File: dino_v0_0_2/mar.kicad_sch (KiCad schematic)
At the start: 5 parts, among them U54 74LS245, U55 74LS373

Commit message: feat(dino): complete v0.0.3 schematic — all 11 sheets netlist-clean
- wire MAR sheet: '373 LO/HI latches, 2x '245 M-bus drive, A15 decode
  (ROM_EN/~RAM_EN), LE stamps off /MAR_LO_LOAD//MAR_HI_LOAD
- fix PC_MAR_MUX polarity: PC '245s enabled on bit14=0, inverted vs
  bit-map convention (PC=1); add ~PC_MAR_MUX inverter, relabel U13/U14
- wire all 7 control-word bus taps [15:9] (SA0-2, END, PC_UP,
  PC_MAR_MUX, HALT) — label pairs had no wire between them
- untie NONE/NC '138 outputs: totem-pole bus fight on every microword;
  each unused output now individually no_connect
- build END (U61 NOR: ~MR = RESET|END, sync T-state clear) and HALT
  (T-state freeze via CET, clock keeps running)
- build COND/JNZ (U62: ~PC_LOAD = taken-JNZ | unconditional-JMP)
- claim src code 111 as /SW_OUT: IN port — DIP switches through 10k
  pull-ups onto W bus via '244; LED bank active-high off OB0-7
- add U66 missing power unit + decouplers (C63-C66)
- tools: kicad_gen_sheet.py (declarative YAML/JSON sheet generator,
  deterministic uuid5, collision-checked), kicad_xsheet_audit.py
  (cross-sheet contract audit); archive stale testing-strategy doc
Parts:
- added C62, C63: 0.1µF, symbol Device:C_Small
- added U58: 74LS373, symbol 74xx:74LS373
- added U59: 74LS245, symbol 74xx:74LS245
- added U60: 74LS02, symbol 74xx:74LS02
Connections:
- net +5V: now also U54.1 (DIR), U54.20 (VCC), U55.20 (VCC), C62.1, C63.1, U58.20 (VCC), U59.1 (DIR), U59.20 (VCC), U60.14 (VCC)
- net GND: now also U54.10 (GND), U55.1 (OE), U55.10 (GND), C62.2, C63.2, U58.1 (OE), U58.10 (GND), U59.10 (GND), U60.7 (GND)
- net M7: now reaches U54.11 (B7)
- net M6: now reaches U54.12 (B6)
- net M5: now reaches U54.13 (B5)
- net M4: now reaches U54.14 (B4)
- net M3: now reaches U54.15 (B3)
- net M2: now reaches U54.16 (B2)
- net M1: now reaches U54.17 (B1)
- net M0: now reaches U54.18 (B0)
- net PC_MAR_MUX: now reaches U54.19 (CE)
- net PC_MAR_MUX: now also U59.19 (CE), U60.11, U60.12
- net MAR0: now reaches U54.2 (A0)
- net MAR0: now also U55.2 (O0)
- net MAR1: now reaches U54.3 (A1)
- net MAR1: now also U55.5 (O1)
- net MAR2: now reaches U54.4 (A2)
- net MAR2: now also U55.6 (O2)
- net MAR3: now reaches U54.5 (A3)
- net MAR3: now also U55.9 (O3)
- net MAR4: now reaches U54.6 (A4)
- net MAR4: now also U55.12 (O4)
- net MAR5: now reaches U54.7 (A5)
- net MAR5: now also U55.15 (O5)
- net MAR6: now reaches U54.8 (A6)
- net MAR6: now also U55.16 (O6)
- net MAR7: now reaches U54.9 (A7)
- net MAR7: now also U55.19 (O7)
- net LE_MAR_LO: now reaches U55.11 (LE)
- net LE_MAR_LO: now also U60.1
- net W4: now reaches U55.13 (D4)
- net W4: now also U58.13 (D4)
- net W5: now reaches U55.14 (D5)
- net W5: now also U58.14 (D5)
- net W6: now reaches U55.17 (D6)
- net W6: now also U58.17 (D6)
- net W7: now reaches U55.18 (D7)
- net W7: now also U58.18 (D7)
- net W0: now reaches U55.3 (D0)
- net W0: now also U58.3 (D0)
- net W1: now reaches U55.4 (D1)
- net W1: now also U58.4 (D1)
- net W2: now reaches U55.7 (D2)
- net W2: now also U58.7 (D2)
- net W3: now reaches U55.8 (D3)
- net W3: now also U58.8 (D3)
- new net CLK: U60.3, U60.6
- new net LE_MAR_HI: U58.11 (LE), U60.4
- new net M10: U59.16 (B2)
- new net M11: U59.15 (B3)
- new net M12: U59.14 (B4)
- new net M13: U59.13 (B5)
- new net M14: U59.12 (B6)
- new net M15: U59.11 (B7), U60.8, U60.9
- new net M8: U59.18 (B0)
- new net M9: U59.17 (B1)
- new net MAR10: U58.6 (O2), U59.4 (A2)
- new net MAR11: U58.9 (O3), U59.5 (A3)
- new net MAR12: U58.12 (O4), U59.6 (A4)
- new net MAR13: U58.15 (O5), U59.7 (A5)
- new net MAR14: U58.16 (O6), U59.8 (A6)
- new net MAR15: U58.19 (O7), U59.9 (A7)
- new net MAR8: U58.2 (O0), U59.2 (A0)
- new net MAR9: U58.5 (O1), U59.3 (A1)
- new net ~{MAR_HI_LOAD}: U60.5
- new net ~{MAR_LO_LOAD}: U60.2
- new net ~{PC_MAR_MUX}: U60.13
- new net ~{RAM_EN}: U60.10

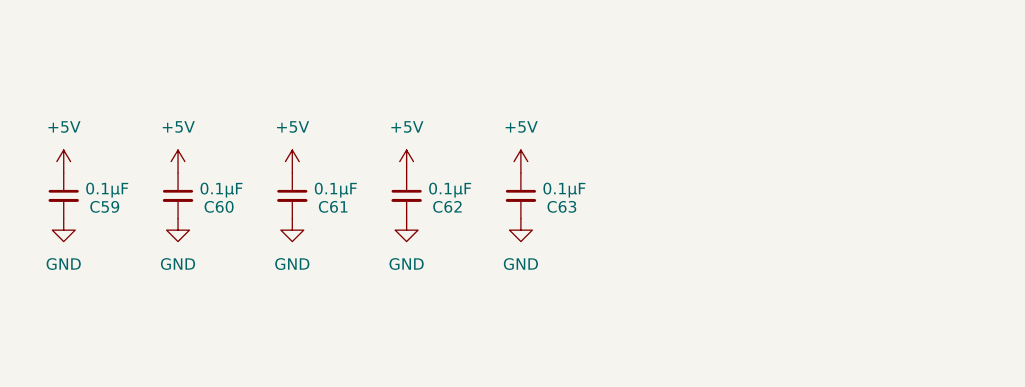
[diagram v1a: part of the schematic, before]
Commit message: feat(dino): generate + stamp per-sheet I/O contracts
Each module's boundary signals (IN/OUT/BIDIR with counterpart sheets)
derived from the kicad-cli netlist and placed as a text block on the
physical sheet, so a bench rig knows exactly what to drive and observe
per board. kicad_contracts.py regenerates both the markdown and the
stamps idempotently; stamping verified electrically neutral.
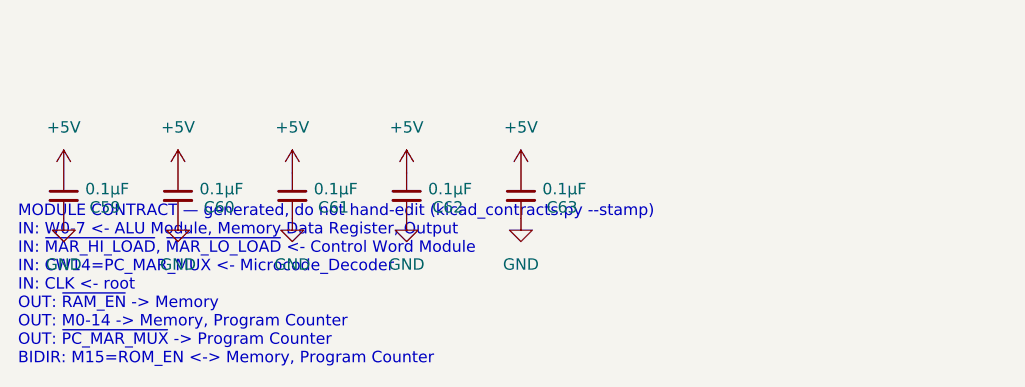
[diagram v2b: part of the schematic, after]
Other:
- note added: "MODULE CONTRACT — generated, do not hand-edit (kicad_contracts.py --stamp) IN: W0-7 <- ALU Module, Memory Data Register, Output IN: ~{MAR_HI_LOAD}, ~{MAR_LO_LOAD} <- Control Word Module IN: CW14=PC_MAR_MUX <- Microcode_Decoder IN: CLK <- root OUT: ~{RAM_EN} -> Memory OUT: M0-14 -> Memory, Program Counter OUT: ~{PC_MAR_MUX} -> Program Counter BIDIR: M15=ROM_EN <-> Memory, Program Counter"
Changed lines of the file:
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@@
+		)
+	)
+	(text "MODULE CONTRACT — generated, do not hand-edit (kicad_contracts.py --stamp)\nIN: W0-7 <- ALU Module, Memory Data Register, Output\nIN: ~{MAR_HI_LOAD}, ~{MAR_LO_LOAD} <- Control Word Module\nIN: CW14=PC_MAR_MUX <- Microcode_Decoder\nIN: CLK <- root\nOUT: ~{RAM_EN} -> Memory\nOUT: M0-14 -> Memory, Program Counter\nOUT: ~{PC_MAR_MUX} -> Program Counter\nBIDIR: M15=ROM_EN <-> Memory, Program Counter"
+		(exclude_from_sim no)
+		(at 15.24 205.58 0)
+		(effects
+			(font
+				(size 1.27 1.27)
+			)
+			(justify left bottom)
 		)
 	)
